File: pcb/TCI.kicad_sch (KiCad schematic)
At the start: 1 part

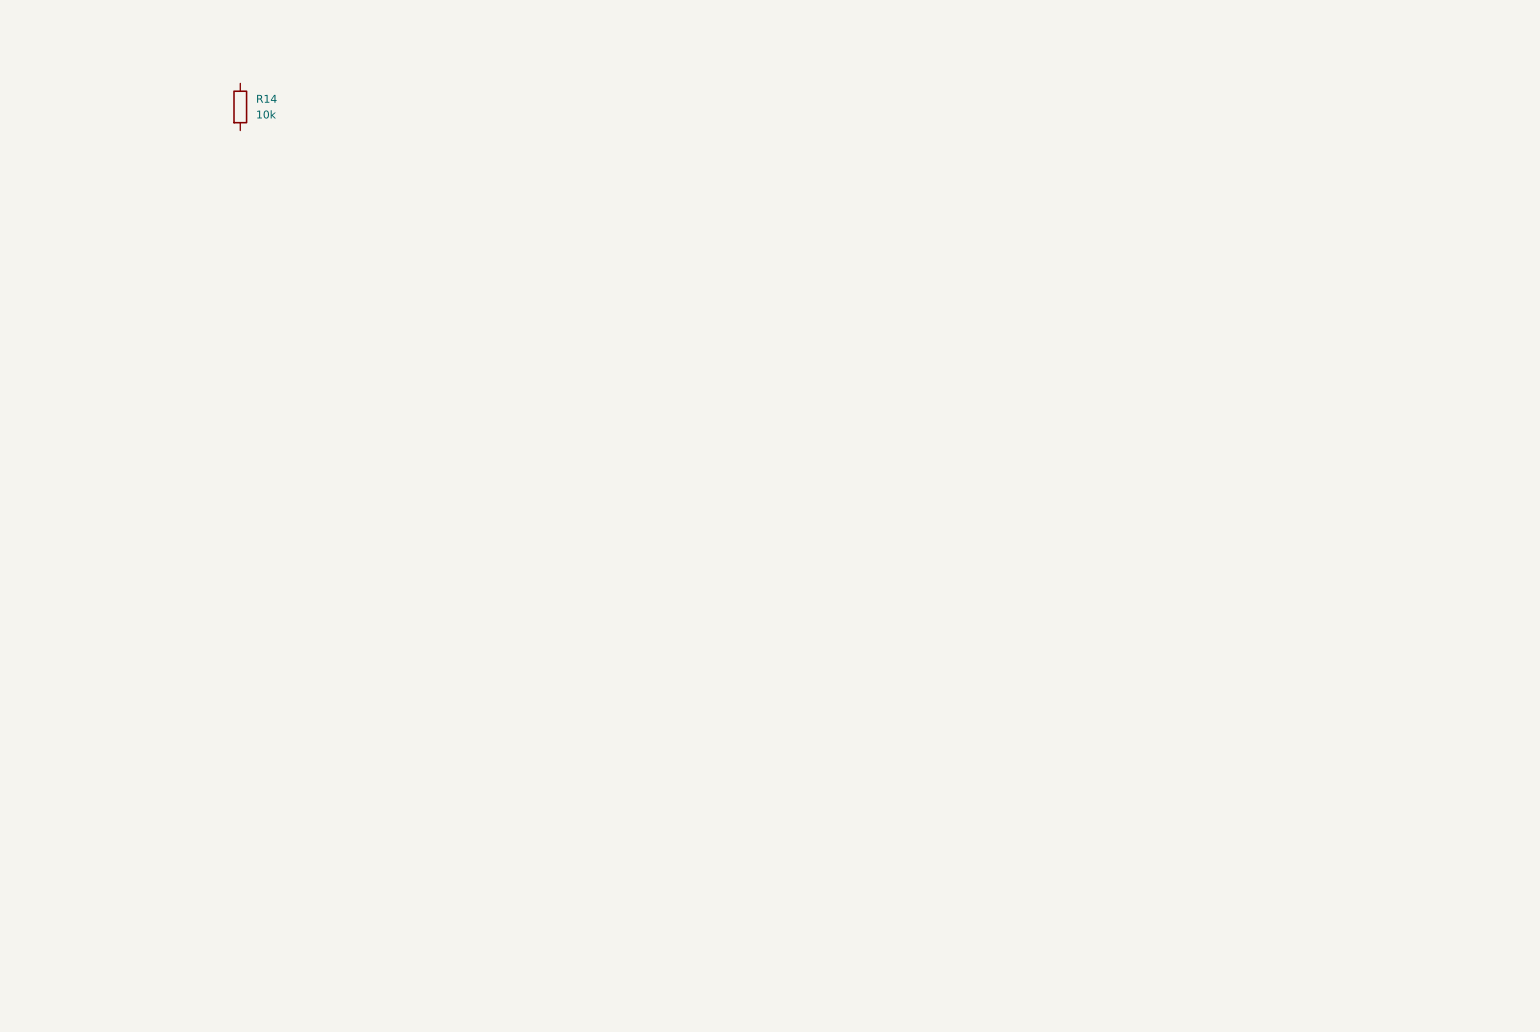
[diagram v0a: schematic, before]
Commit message: implemented TCI quickshifter
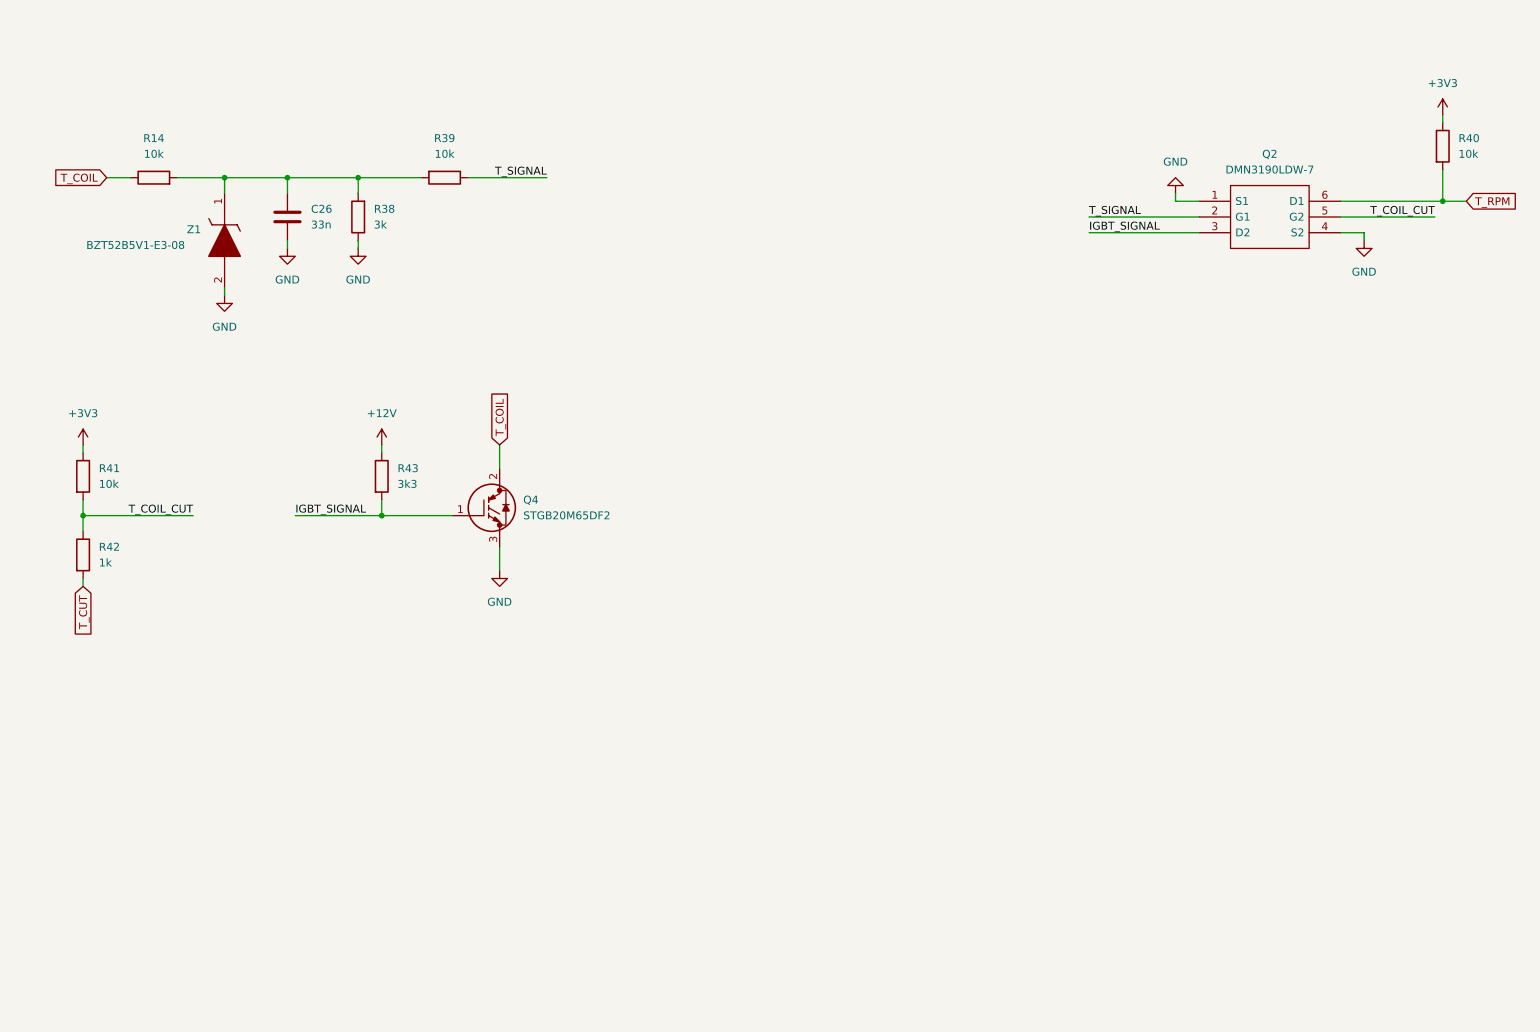
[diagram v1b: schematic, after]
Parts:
- added C26: 33n, symbol Device:C
- added Q2: DMN3190LDW-7, SOT65P210X110-6N, symbol SamacSys_Parts:DMN3190LDW-7
- added Q4: STGB20M65DF2, STGB20M65DF2, symbol SamacSys_Parts:STGB20M65DF2
- added R38: 3k, Resistor_SMD:R_0201_0603Metric, symbol Device:R
- added R39, R40, R41: 10k, Resistor_SMD:R_0201_0603Metric, symbol Device:R
- added R42: 1k, Resistor_SMD:R_0201_0603Metric, symbol Device:R
- added R43: 3k3, Resistor_SMD:R_0201_0603Metric, symbol Device:R
- added Z1: BZT52B5V1-E3-08, BZT52B5V1E308, symbol SamacSys_Parts:BZT52B5V1-E3-08
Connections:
- net T_COIL: now reaches R14.1
- net T_COIL: now also Q4.2
- net at R14.2: now also C26.1, R38.2, R39.2, Z1.1
- new net +12V: R43.1
- new net +3V3: R40.1, R41.1
- new net GND: C26.2, Q2.1 (S1), Q2.4 (S2), Q4.3, R38.1, Z1.2
- new net IGBT_SIGNAL: Q2.3 (D2), Q4.1, R43.2
- new net T_COIL_CUT: Q2.5 (G2), R41.2, R42.1
- new net T_CUT: R42.2
- new net T_RPM: Q2.6 (D1), R40.2
- new net T_SIGNAL: Q2.2 (G1), R39.1
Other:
- moved on the sheet: R14

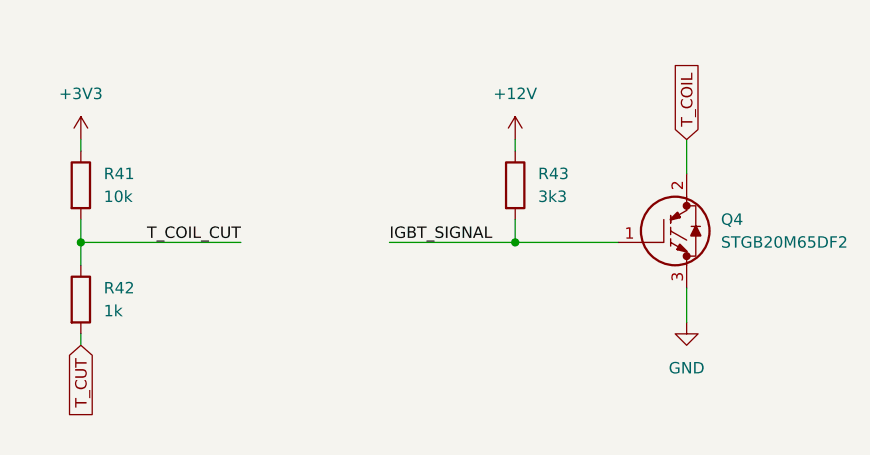
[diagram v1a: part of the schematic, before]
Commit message: fixed IGBT logic
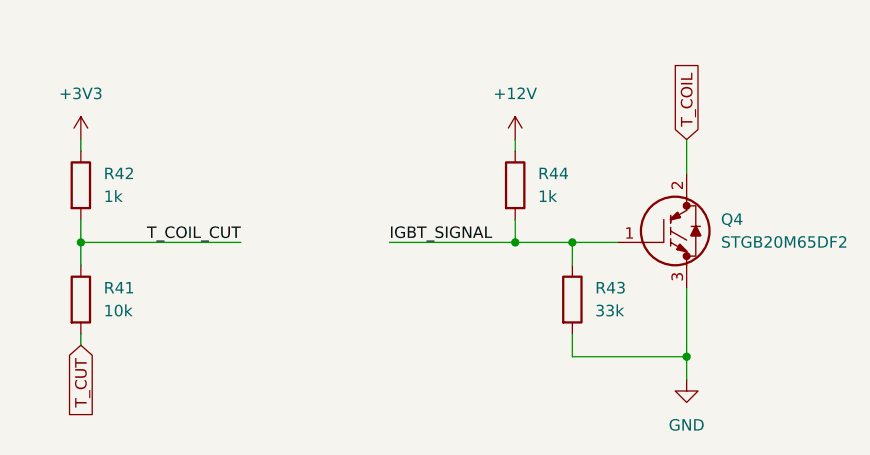
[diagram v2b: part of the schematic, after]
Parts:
- added R44: 1k, Resistor_SMD:R_0201_0603Metric, symbol Device:R
- R43: value 3k3 -> 33k
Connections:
- net +12V: now also R44.1; no longer R43.1
- net +3V3: now also R42.1; no longer R41.1
- net GND: now also R43.2
- net IGBT_SIGNAL: now also R43.1, R44.2; no longer R43.2
- net T_COIL_CUT: now also R41.1, R42.2; no longer R41.2, R42.1
- net T_CUT: now also R41.2; no longer R42.2
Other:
- moved on the sheet: R41, R42, R43
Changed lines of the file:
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@@
 	(paper "A4")
+	(junction
+		(at 101.6 118.11)
+		(diameter 0)
+		(color 0 0 0 0)
+	)
+	(junction
+		(at 88.9 105.41)
+		(diameter 0)
+		(color 0 0 0 0)
+	)
 	(junction
 		(at 67.31 50.8)
@@
 	(wire
 		(pts
+			(xy 88.9 115.57) (xy 88.9 118.11)
+		)
+		(stroke
+			(width 0)
+			(type default)
+		)
+	)
+	(wire
+		(pts
+			(xy 101.6 118.11) (xy 101.6 110.49)
+		)
+		(stroke
+			(width 0)
+			(type default)
+		)
+	)
+	(wire
+		(pts
 			(xy 196.85 59.69) (xy 214.63 59.69)
 		)
@@
 	(wire
 		(pts
+			(xy 88.9 118.11) (xy 101.6 118.11)
+		)
+		(stroke
+			(width 0)
+			(type default)
+		)
+	)
+	(wire
+		(pts
 			(xy 67.31 50.8) (xy 78.74 50.8)
 		)
@@
 	(wire
 		(pts
+			(xy 88.9 107.95) (xy 88.9 105.41)
+		)
+		(stroke
+			(width 0)
+			(type default)
+		)
+	)
+	(wire
+		(pts
 			(xy 78.74 53.34) (xy 78.74 50.8)
 		)
@@
 	(wire
 		(pts
-			(xy 82.55 105.41) (xy 93.98 105.41)
+			(xy 82.55 105.41) (xy 88.9 105.41)
 		)
 		(stroke
@@
 	(wire
 		(pts
+			(xy 88.9 105.41) (xy 93.98 105.41)
+		)
+		(stroke
+			(width 0)
+			(type default)
+		)
+	)
+	(wire
+		(pts
 			(xy 210.82 53.34) (xy 210.82 54.61)
 		)
@@
 	(wire
 		(pts
-			(xy 101.6 114.3) (xy 101.6 110.49)
+			(xy 101.6 120.65) (xy 101.6 118.11)
 		)
 		(stroke
@@
 	(symbol
 		(lib_id "Device:R")
+		(at 34.29 111.76 0)
+		(unit 1)
+		(exclude_from_sim no)
+		(in_bom yes)
+		(on_board yes)
+		(dnp no)
+		(fields_autoplaced yes)
+		(property "Reference" "R41"
+			(at 36.83 110.4899 0)
+			(effects
+				(font
+					(size 1.27 1.27)
+				)
+				(justify left)
+			)
+		)
+		(property "Value" "10k"
+			(at 36.83 113.0299 0)
+			(effects
+				(font
+					(size 1.27 1.27)
+				)
+				(justify left)
+			)
+		)
+		(property "Footprint" "Resistor_SMD:R_0201_0603Metric"
+			(at 32.512 111.76 90)
+			(effects
+				(font
+					(size 1.27 1.27)
+				)
+				(hide yes)
+			)
+		)
+		(property "Datasheet" "~"
+			(at 34.29 111.76 0)
+			(effects
+				(font
+					(size 1.27 1.27)
+				)
+				(hide yes)
+			)
+		)
+		(property "Description" "Resistor"
+			(at 34.29 111.76 0)
+			(effects
+				(font
+					(size 1.27 1.27)
+				)
+				(hide yes)
+			)
+		)
+		(pin "1"
+		)
+		(pin "2"
+		)
+		(instances
+			(project "ecu-dev-board"
+				(path "/38d4df77-b5a0-4642-8410-8b13c21c2c3b/1f135221-d921-46ea-b769-b97fce3b730c"
+					(reference "R41")
+					(unit 1)
+				)
+			)
+		)
+	)
+	(symbol
+		(lib_id "Device:R")
 		(at 34.29 99.06 0)
 		(unit 1)
@@
 		(dnp no)
 		(fields_autoplaced yes)
-		(property "Reference" "R41"
+		(property "Reference" "R42"
 			(at 36.83 97.7899 0)
 			(effects
@@
 			)
 		)
-		(property "Value" "10k"
+		(property "Value" "1k"
 			(at 36.83 100.3299 0)
 			(effects
@@
 		(property "Description" "Resistor"
 			(at 34.29 99.06 0)
-			(effects
-				(font
-					(size 1.27 1.27)
-				)
-				(hide yes)
-			)
-		)
-		(pin "1"
-		)
-		(pin "2"
-		)
-		(instances
-			(project "ecu-dev-board"
-				(path "/38d4df77-b5a0-4642-8410-8b13c21c2c3b/1f135221-d921-46ea-b769-b97fce3b730c"
-					(reference "R41")
-					(unit 1)
-				)
-			)
-		)
-	)
-	(symbol
-		(lib_id "Device:R")
-		(at 34.29 111.76 0)
-		(unit 1)
-		(exclude_from_sim no)
-		(in_bom yes)
-		(on_board yes)
-		(dnp no)
-		(fields_autoplaced yes)
-		(property "Reference" "R42"
-			(at 36.83 110.4899 0)
-			(effects
-				(font
-					(size 1.27 1.27)
-				)
-				(justify left)
-			)
-		)
-		(property "Value" "1k"
-			(at 36.83 113.0299 0)
-			(effects
-				(font
-					(size 1.27 1.27)
-				)
-				(justify left)
-			)
-		)
-		(property "Footprint" "Resistor_SMD:R_0201_0603Metric"
-			(at 32.512 111.76 90)
-			(effects
-				(font
-					(size 1.27 1.27)
-				)
-				(hide yes)
-			)
-		)
-		(property "Datasheet" "~"
-			(at 34.29 111.76 0)
-			(effects
-				(font
-					(size 1.27 1.27)
-				)
-				(hide yes)
-			)
-		)
-		(property "Description" "Resistor"
-			(at 34.29 111.76 0)
 			(effects
 				(font
@@
 	)
 	(symbol
-		(lib_id "power:GND")
-		(at 101.6 114.3 0)
-		(unit 1)
-		(exclude_from_sim no)
-		(in_bom yes)
-		(on_board yes)
-		(dnp no)
-		(fields_autoplaced yes)
-		(property "Reference" "#PWR046"
-			(at 101.6 120.65 0)
-			(effects
-				(font
-					(size 1.27 1.27)
-				)
-				(hide yes)
-			)
-		)
-		(property "Value" "GND"
-			(at 101.6 119.38 0)
-			(effects
-				(font
-					(size 1.27 1.27)
-				)
-			)
-		)
-		(property "Footprint" ""
-			(at 101.6 114.3 0)
-			(effects
-				(font
-					(size 1.27 1.27)
-				)
-				(hide yes)
-			)
-		)
-		(property "Datasheet" ""
-			(at 101.6 114.3 0)
-			(effects
-				(font
-					(size 1.27 1.27)
-				)
-				(hide yes)
-			)
-		)
-		(property "Description" "Power symbol creates a global label with name \"GND\" , ground"
-			(at 101.6 114.3 0)
-			(effects
-				(font
-					(size 1.27 1.27)
-				)
-				(hide yes)
-			)
-		)
-		(pin "1"
-		)
-		(instances
-			(project "ecu-dev-board"
-				(path "/38d4df77-b5a0-4642-8410-8b13c21c2c3b/1f135221-d921-46ea-b769-b97fce3b730c"
-					(reference "#PWR046")
-					(unit 1)
-				)
-			)
-		)
-	)
-	(symbol
 		(lib_id "Device:R")
 		(at 82.55 99.06 0)
@@
 		(dnp no)
 		(fields_autoplaced yes)
-		(property "Reference" "R43"
+		(property "Reference" "R44"
 			(at 85.09 97.7899 0)
 			(effects
@@
 			)
 		)
-		(property "Value" "3k3"
+		(property "Value" "1k"
 			(at 85.09 100.3299 0)
 			(effects
@@
 			(effects
 				(font
+					(size 1.27 1.27)
+				)
+				(hide yes)
+			)
+		)
+		(pin "1"
+		)
+		(pin "2"
+		)
+		(instances
+			(project "ecu-dev-board"
+				(path "/38d4df77-b5a0-4642-8410-8b13c21c2c3b/1f135221-d921-46ea-b769-b97fce3b730c"
+					(reference "R44")
+					(unit 1)
+				)
+			)
+		)
+	)
+	(symbol
+		(lib_id "power:GND")
+		(at 101.6 120.65 0)
+		(unit 1)
+		(exclude_from_sim no)
+		(in_bom yes)
+		(on_board yes)
+		(dnp no)
+		(fields_autoplaced yes)
+		(property "Reference" "#PWR046"
+			(at 101.6 127 0)
+			(effects
+				(font
+					(size 1.27 1.27)
+				)
+				(hide yes)
+			)
+		)
+		(property "Value" "GND"
+			(at 101.6 125.73 0)
+			(effects
+				(font
+					(size 1.27 1.27)
+				)
+			)
+		)
+		(property "Footprint" ""
+			(at 101.6 120.65 0)
+			(effects
+				(font
+					(size 1.27 1.27)
+				)
+				(hide yes)
+			)
+		)
+		(property "Datasheet" ""
+			(at 101.6 120.65 0)
+			(effects
+				(font
+					(size 1.27 1.27)
+				)
+				(hide yes)
+			)
+		)
+		(property "Description" "Power symbol creates a global label with name \"GND\" , ground"
+			(at 101.6 120.65 0)
+			(effects
+				(font
+					(size 1.27 1.27)
+				)
+				(hide yes)
+			)
+		)
+		(pin "1"
+		)
+		(instances
+			(project "ecu-dev-board"
+				(path "/38d4df77-b5a0-4642-8410-8b13c21c2c3b/1f135221-d921-46ea-b769-b97fce3b730c"
+					(reference "#PWR046")
+					(unit 1)
+				)
+			)
+		)
+	)
+	(symbol
+		(lib_id "Device:R")
+		(at 88.9 111.76 0)
+		(unit 1)
+		(exclude_from_sim no)
+		(in_bom yes)
+		(on_board yes)
+		(dnp no)
+		(fields_autoplaced yes)
+		(property "Reference" "R43"
+			(at 91.44 110.4899 0)
+			(effects
+				(font
+					(size 1.27 1.27)
+				)
+				(justify left)
+			)
+		)
+		(property "Value" "33k"
+			(at 91.44 113.0299 0)
+			(effects
+				(font
+					(size 1.27 1.27)
+				)
+				(justify left)
+			)
+		)
+		(property "Footprint" "Resistor_SMD:R_0201_0603Metric"
+			(at 87.122 111.76 90)
+			(effects
+				(font
+					(size 1.27 1.27)
+				)
+				(hide yes)
+			)
+		)
+		(property "Datasheet" "~"
+			(at 88.9 111.76 0)
+			(effects
+				(font
+					(size 1.27 1.27)
+				)
+				(hide yes)
+			)
+		)
+		(property "Description" "Resistor"
+			(at 88.9 111.76 0)
+			(effects
+				(font

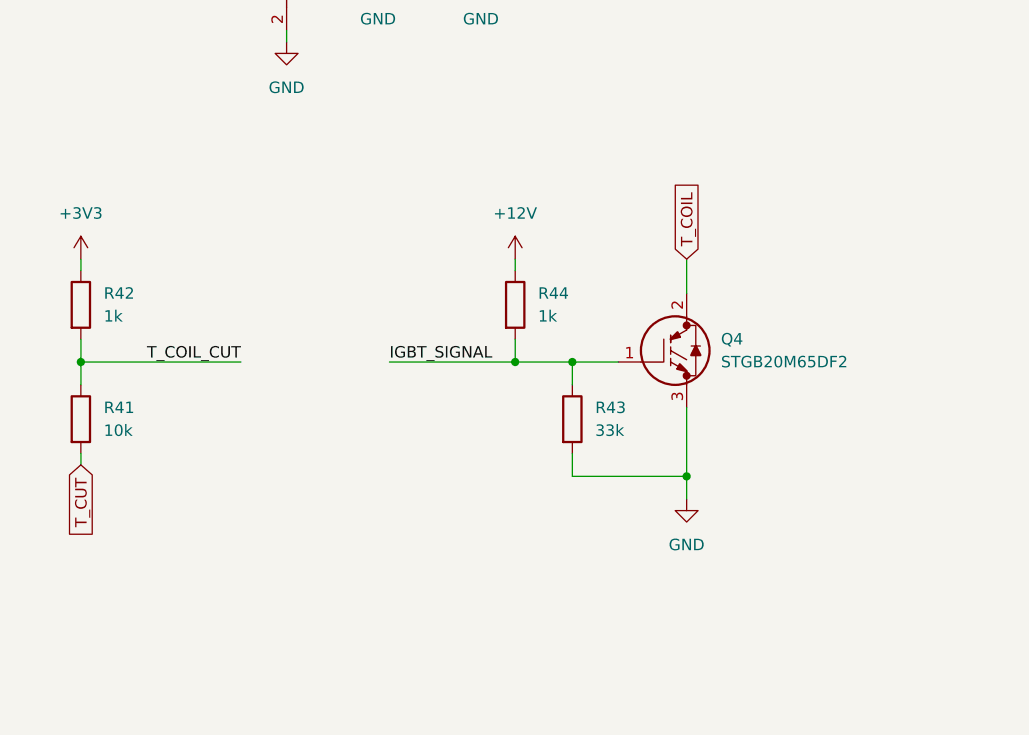
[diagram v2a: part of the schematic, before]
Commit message: added footprints
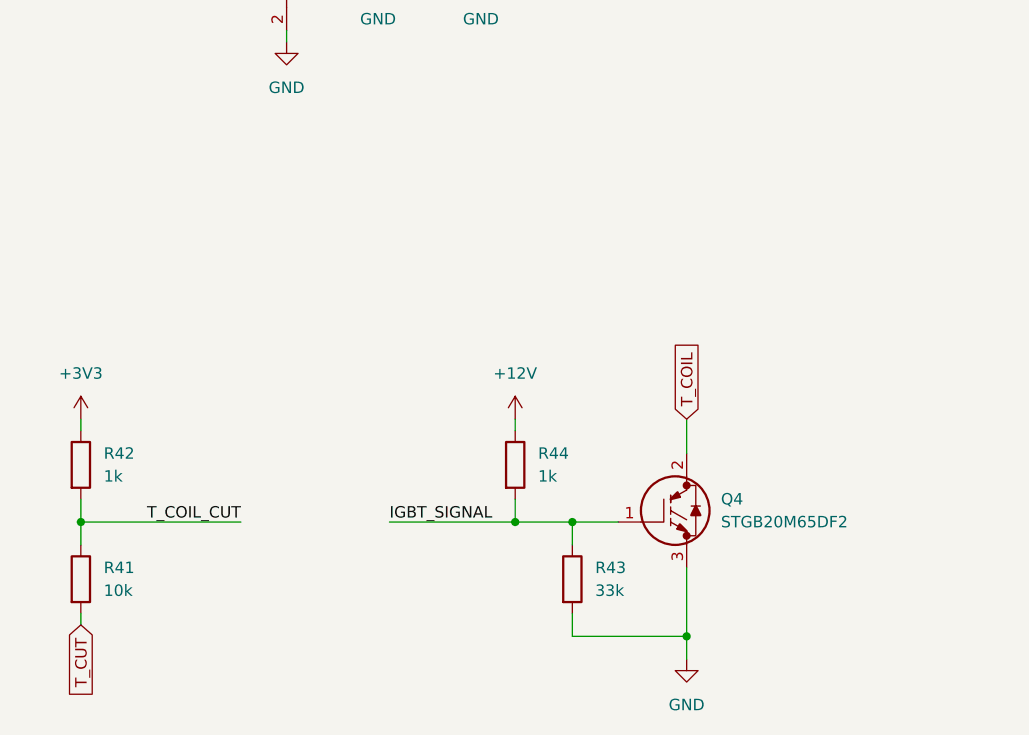
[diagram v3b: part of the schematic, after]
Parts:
- C26: footprint (none) -> Capacitor_SMD:C_0201_0603Metric
- Q2: footprint SOT65P210X110-6N -> SamacSys_Parts:SOT65P210X110-6N
- Q4: footprint STGB20M65DF2 -> SamacSys_Parts:STGB20M65DF2
- Z1: footprint BZT52B5V1E308 -> SamacSys_Parts:BZT52B5V1E308
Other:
- moved on the sheet: Q4, R41, R42, R43, R44

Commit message: changed capacitors and resistors footprints from 0201 to 0603
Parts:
- C26: footprint Capacitor_SMD:C_0201_0603Metric -> Capacitor_SMD:C_0603_1608Metric
- R14, R38, R39, R40, R41, R42, R43, R44: footprint Resistor_SMD:R_0201_0603Metric -> Resistor_SMD:R_0603_1608Metric
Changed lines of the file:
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@@
 			)
 		)
-		(property "Footprint" "Capacitor_SMD:C_0201_0603Metric"
+		(property "Footprint" "Capacitor_SMD:C_0603_1608Metric"
 			(at 68.2752 60.96 0)
 			(effects
@@
 			)
 		)
-		(property "Footprint" "Resistor_SMD:R_0201_0603Metric"
+		(property "Footprint" "Resistor_SMD:R_0603_1608Metric"
 			(at 80.518 57.15 90)
 			(effects
@@
 			)
 		)
-		(property "Footprint" "Resistor_SMD:R_0201_0603Metric"
+		(property "Footprint" "Resistor_SMD:R_0603_1608Metric"
 			(at 32.512 129.54 90)
 			(effects
@@
 			)
 		)
-		(property "Footprint" "Resistor_SMD:R_0201_0603Metric"
+		(property "Footprint" "Resistor_SMD:R_0603_1608Metric"
 			(at 32.512 116.84 90)
 			(effects
@@
 			)
 		)
-		(property "Footprint" "Resistor_SMD:R_0201_0603Metric"
+		(property "Footprint" "Resistor_SMD:R_0603_1608Metric"
 			(at 252.222 45.72 90)
 			(effects
@@
 			)
 		)
-		(property "Footprint" "Resistor_SMD:R_0201_0603Metric"
+		(property "Footprint" "Resistor_SMD:R_0603_1608Metric"
 			(at 45.72 52.578 90)
 			(effects
@@
 			)
 		)
-		(property "Footprint" "Resistor_SMD:R_0201_0603Metric"
+		(property "Footprint" "Resistor_SMD:R_0603_1608Metric"
 			(at 92.71 49.022 90)
 			(effects
@@
 			)
 		)
-		(property "Footprint" "Resistor_SMD:R_0201_0603Metric"
+		(property "Footprint" "Resistor_SMD:R_0603_1608Metric"
 			(at 80.772 116.84 90)
 			(effects
@@
 			)
 		)
-		(property "Footprint" "Resistor_SMD:R_0201_0603Metric"
+		(property "Footprint" "Resistor_SMD:R_0603_1608Metric"
 			(at 87.122 129.54 90)
 			(effects
